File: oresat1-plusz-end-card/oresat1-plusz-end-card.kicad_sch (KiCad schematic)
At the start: 34 parts, among them J1 J-SAMTEC-TFM-120-01-L-D-RA, J2 M55-7101242R, J3 M55-7101242R, J4 M55-7101242R, J5 M55-7101242R, J6 U.FL-R-SMT-1

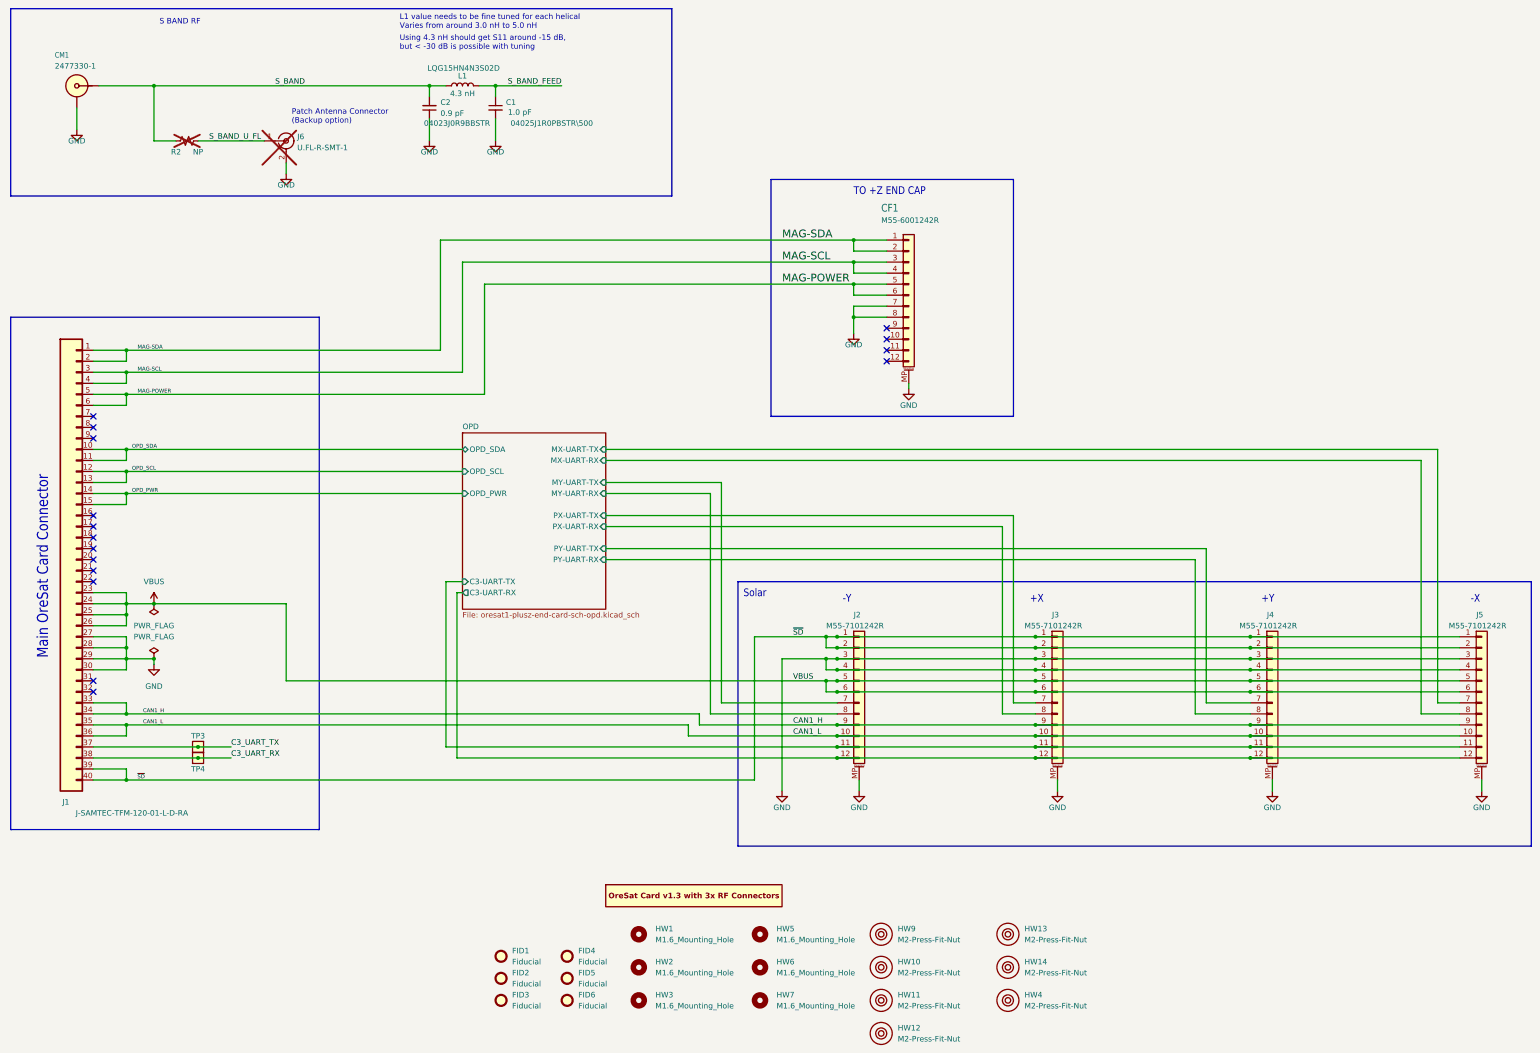
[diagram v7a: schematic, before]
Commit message: Fixed weird footprint sync error that kept popping up on DRC around the mounting holes because of the polygon zone keepout areas. Also found a huge mistake in the schematic, fixed, still needs to be routed.
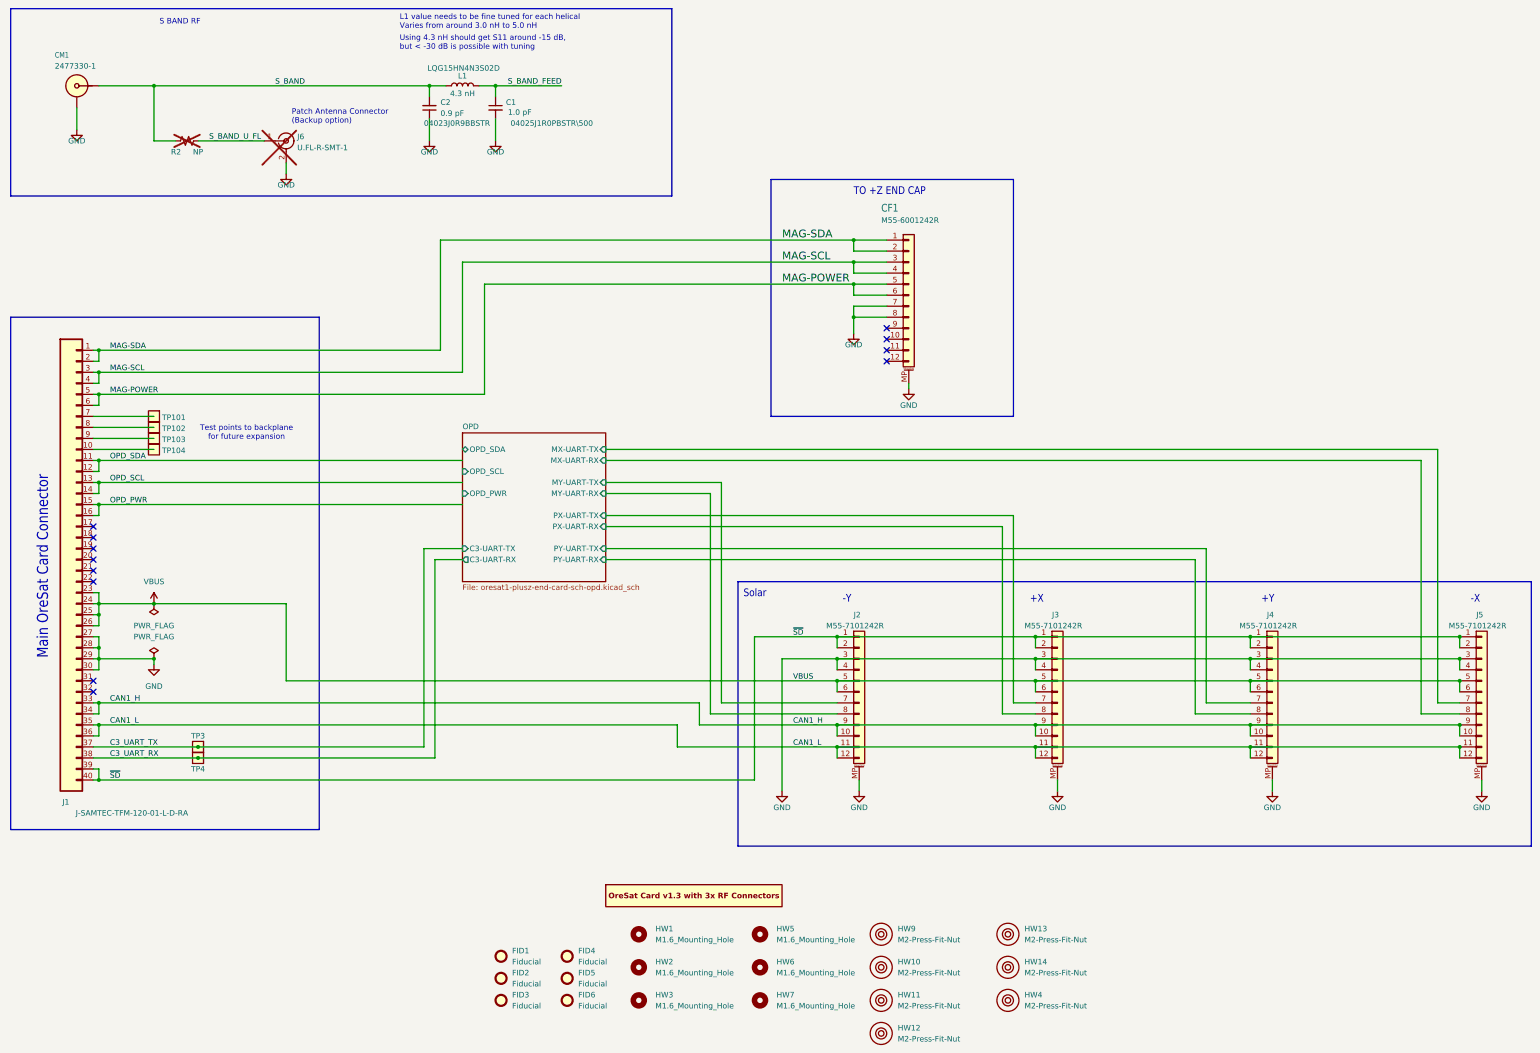
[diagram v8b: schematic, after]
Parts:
- added TP101, TP102, TP103, TP104: TestPoint-MinTH, oresat-misc:TestPoint-0.75mm-th, symbol oresat-misc:Test-Point-0.75mm-th
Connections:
- net OPD/C3-UART-RX is gone; now on net CAN1_L: J2.12 (Pin_12), J3.12 (Pin_12), J4.12 (Pin_12), J5.12 (Pin_12)
- net OPD/C3-UART-TX is gone; now on net CAN1_L: J2.11 (Pin_11), J3.11 (Pin_11), J4.11 (Pin_11), J5.11 (Pin_11)
- net CAN1_H: now also J2.10 (Pin_10), J3.10 (Pin_10), J4.10 (Pin_10), J5.10 (Pin_10)
- net CAN1_L: no longer J2.10 (Pin_10), J3.10 (Pin_10), J4.10 (Pin_10), J5.10 (Pin_10)
- net OPD_PWR: now also J1.16; no longer J1.14
- net OPD_SCL: now also J1.14; no longer J1.12
- net OPD_SDA: now also J1.12; no longer J1.10
- net at J1.7: now also TP101.1
- net at J1.8: now also TP102.1
- net at J1.9: now also TP103.1
- new net: J1.10, TP104.1
- no-connect marks 16 -> 12
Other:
- note added: "Test points to backplane for future expansion"
